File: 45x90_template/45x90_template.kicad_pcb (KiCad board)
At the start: 2 copper layers, 90 x 45 mm, 9 parts, among them J1 Screw_Terminal_01x02

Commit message: Templates updated.
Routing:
- removed copper zone on B.Cu, net 0
- removed copper zone on F.Cu, net 0

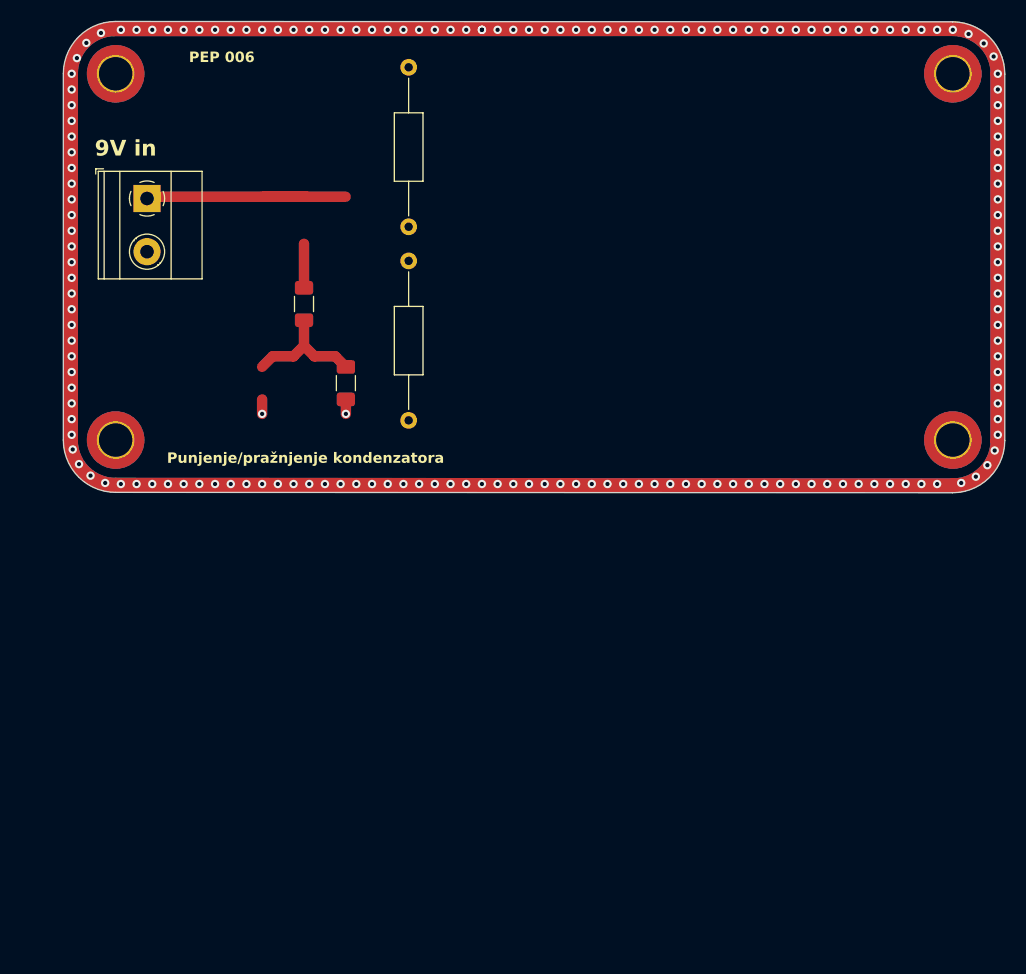
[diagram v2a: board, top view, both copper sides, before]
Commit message: PEP004 and template 90 update.
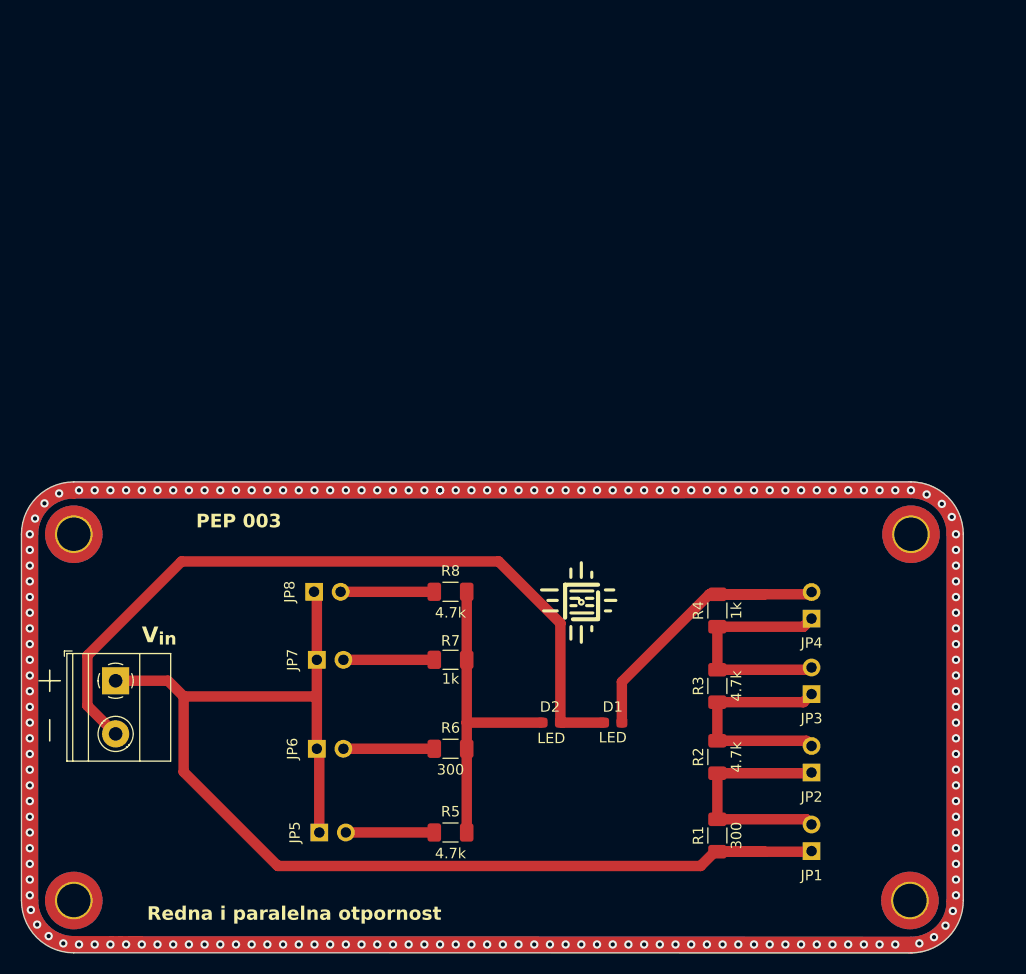
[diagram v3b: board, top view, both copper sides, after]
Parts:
- added D1: LED, LED_SMD:LED_0603_1608Metric_Pad1.05x0.95mm_HandSolder, F.Cu at (156.5, 128.0)
- added D2: LED, LED_SMD:LED_0603_1608Metric_Pad1.05x0.95mm_HandSolder, F.Cu at (150.6, 128.0)
- added G***: LOGO, logo:logo, B.Cu at (153.5, 116.5)
- added JP1: Jumper, Connector_PinHeader_2.54mm:PinHeader_1x02_P2.54mm_Vertical, F.Cu at (175.5, 140.3)
- added JP2: Jumper, Connector_PinHeader_2.54mm:PinHeader_1x02_P2.54mm_Vertical, F.Cu at (175.5, 132.8)
- added JP3: Jumper, Connector_PinHeader_2.54mm:PinHeader_1x02_P2.54mm_Vertical, F.Cu at (175.5, 125.3)
- added JP4: Jumper, Connector_PinHeader_2.54mm:PinHeader_1x02_P2.54mm_Vertical, F.Cu at (175.5, 118.1)
- added JP5: Jumper, Connector_PinHeader_2.54mm:PinHeader_1x02_P2.54mm_Vertical, F.Cu at (128.5, 138.5)
- added JP6: Jumper, Connector_PinHeader_2.54mm:PinHeader_1x02_P2.54mm_Vertical, F.Cu at (128.2, 130.5)
- added JP7: Jumper, Connector_PinHeader_2.54mm:PinHeader_1x02_P2.54mm_Vertical, F.Cu at (128.2, 122.0)
- added JP8: Jumper, Connector_PinHeader_2.54mm:PinHeader_1x02_P2.54mm_Vertical, F.Cu at (128.0, 115.5)
- added R5: 4.7k, PEP_library:R_smd, F.Cu at (141.0, 138.5)
- added R6: 300, PEP_library:R_smd, F.Cu at (141.0, 130.5)
- added R7: 1k, PEP_library:R_smd, F.Cu at (141.0, 122.0)
- added R8: 4.7k, PEP_library:R_smd, F.Cu at (141.0, 115.5)
- added REF**: ele_petnica_logo, PEP_library:ele_petnica_logo, F.Cu at (153.5, 116.5)
- added REF**: JP_silk_symbol, PEP_library:JP_silk_symbol, F.Cu at (131.5, 139.6)
- added REF**: JP_silk_symbol, PEP_library:JP_silk_symbol, F.Cu at (131.4, 131.6)
- added REF**: JP_silk_symbol, PEP_library:JP_silk_symbol, F.Cu at (131.5, 115.1)
- added REF**: R_silk_symbol, PEP_library:R_silk_symbol, F.Cu at (166.4, 134.1)
- added REF**: JP_silk_symbol, PEP_library:JP_silk_symbol, F.Cu at (175.5, 124.5)
- added REF**: R_silk_symbol, PEP_library:R_silk_symbol, F.Cu at (166.4, 126.6)
- added REF**: JP_silk_symbol, PEP_library:JP_silk_symbol, F.Cu at (175.5, 116.8)
- added REF**: JP_silk_symbol, PEP_library:JP_silk_symbol, F.Cu at (131.5, 123.6)
- added REF**: JP_silk_symbol, PEP_library:JP_silk_symbol, F.Cu at (175.5, 139.0)
- added REF**: R_silk_symbol, PEP_library:R_silk_symbol, F.Cu at (166.4, 119.3)
- added REF**: JP_silk_symbol, PEP_library:JP_silk_symbol, F.Cu at (175.5, 131.5)
- added REF**: R_silk_symbol, PEP_library:R_silk_symbol, F.Cu at (166.4, 112.6)
- added REF**: R_silk_symbol, PEP_library:R_silk_symbol, F.Cu at (133.3, 123.6)
- added REF**: R_silk_symbol, PEP_library:R_silk_symbol, F.Cu at (133.3, 139.6)
- added REF**: R_silk_symbol, PEP_library:R_silk_symbol, F.Cu at (133.3, 131.6)
- added REF**: R_silk_symbol, PEP_library:R_silk_symbol, F.Cu at (133.3, 115.1)
- J1: footprint TerminalBlock_Phoenix:TerminalBlock_Phoenix_MKDS-1,5-2-5.08_1x02_P5.08mm_Horizontal -> PEP_library:TerminalBlock_Phoenix_MKDS-1,5-2-5.08_1x02_P5.08mm_Horizontal
- R1: value 100k -> 300; footprint Resistor_SMD:R_1206_3216Metric_Pad1.30x1.75mm_HandSolder -> PEP_library:R_smd
- R2: value 100k -> 4.7k; footprint Resistor_SMD:R_1206_3216Metric_Pad1.30x1.75mm_HandSolder -> PEP_library:R_smd
- R3: value 100k -> 4.7k; footprint Resistor_THT:R_Axial_DIN0207_L6.3mm_D2.5mm_P15.24mm_Horizontal -> PEP_library:R_smd
- R4: value 100k -> 1k; footprint Resistor_THT:R_Axial_DIN0207_L6.3mm_D2.5mm_P15.24mm_Horizontal -> PEP_library:R_smd
- moved R4 59.7 mm to (166.5, 117.3), turned to 90 degrees
- moved R2 58.6 mm to (166.5, 131.3), turned to 90 degrees
- moved R1 55.9 mm to (166.5, 138.8), turned to 90 degrees
- moved J1 46.2 mm to (109.0, 124.0)
- moved H4 44.2 mm to (184.9, 145.0)
- moved H1 44.2 mm to (105.0, 145.0)
- moved H2 44.2 mm to (105.0, 110.0)
- moved H3 44.2 mm to (185.0, 110.0)
- moved R3 38.9 mm to (166.5, 124.5)
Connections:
- R1 pad 1: out -> 9V
- R1 pad 2: 0 -> Net-(JP1-B)
- R2 pad 1: 9V -> Net-(JP1-B)
- R2 pad 2: out -> Net-(JP2-B)
- R3 pad 1: Net-(R3-Pad1) -> Net-(JP2-B)
- R3 pad 2: 0 -> Net-(JP3-B)
- R4 pad 1: Net-(R3-Pad1) -> Net-(JP3-B)
- R4 pad 2: 9V -> Net-(D1-A)
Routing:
- net 9V: track 27.5 -> 119.1 mm
- net 0: track 2.76 -> 73.7 mm, vias 172 -> 0
- net Net-(D2-A): track 0.00 -> 30.2 mm
- net Net-(D1-A): track 0.00 -> 30.1 mm
- net Net-(JP1-B): track 0.00 -> 22.6 mm
- net Net-(JP3-B): track 0.00 -> 22.5 mm
- net Net-(JP2-B): track 0.00 -> 22.2 mm
- net out: track 12.1 -> 0.00 mm
- net Net-(JP8-B): track 0.00 -> 8.95 mm
- net Net-(JP7-B): track 0.00 -> 8.69 mm
- net Net-(JP6-B): track 0.00 -> 8.69 mm
- net Net-(JP5-B): track 0.00 -> 8.45 mm
- net (no net): vias 0 -> 170
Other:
- board text added: "PEP 003"
- board text added: "Redna i paralelna otpornost"
- board text added: "V_{in}"
- board text removed: "9V in"
- board text removed: "PEP 006"
- board text removed: "Punjenje/pražnjenje kondenzatora"
